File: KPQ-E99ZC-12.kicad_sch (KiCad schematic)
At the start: 23 parts, among them J1 USB, J2 Chassis, J3 SWD, J4 Edge Connector, J5 Alternate Connector, SW1 BOOT, U1 USBLC6-2SC6, U2 XC6206P332MR-G, U3 STM32C071KBT6

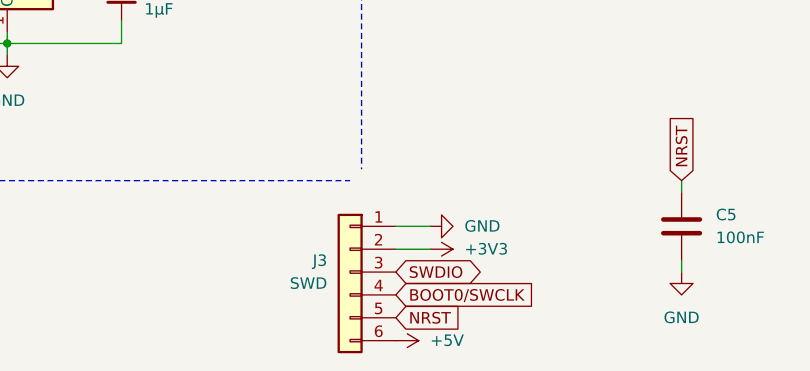
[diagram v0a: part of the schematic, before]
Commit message: Remove +5V from J3
This can be accessed via J1, and would avoid +5V being input from both J1 and J3 at the same time.
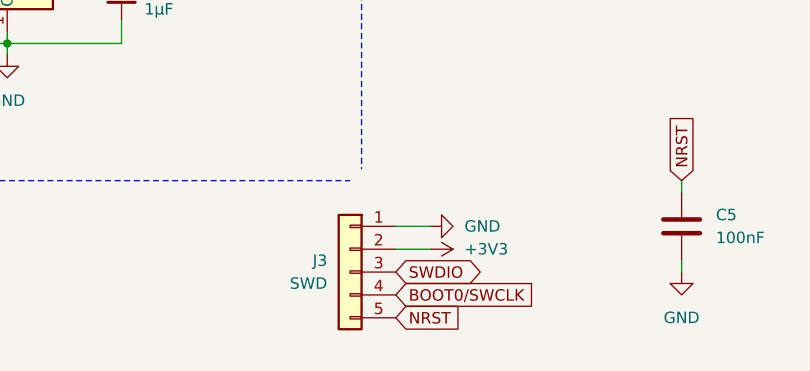
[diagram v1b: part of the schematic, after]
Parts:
- J3: footprint Connector_PinHeader_2.54mm:PinHeader_1x06_P2.54mm_Vertical -> Connector_PinHeader_2.54mm:PinHeader_1x05_P2.54mm_Vertical; symbol Connector_Generic:Conn_01x06 -> Connector_Generic:Conn_01x05; P6 +5V -> (none)
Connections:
- net +5V: no longer J3.6 (Pin_6)
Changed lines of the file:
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@@
-	)
-	(symbol
-		(lib_id "power:+5V")
-		(at 83.82 193.04 270)
-		(unit 1)
-		(exclude_from_sim no)
-		(in_bom yes)
-		(on_board yes)
-		(dnp no)
-		(fields_autoplaced yes)
-		(property "Reference" "#PWR032"
-			(at 80.01 193.04 0)
-			(effects
-				(font
-					(size 1.27 1.27)
-				)
-				(hide yes)
-			)
-		)
-		(property "Value" "+5V"
-			(at 87.63 193.04 90)
-			(effects
-				(font
-					(size 1.27 1.27)
-				)
-				(justify left)
-			)
-		)
-		(property "Footprint" ""
-			(at 83.82 193.04 0)
-			(effects
-				(font
-					(size 1.27 1.27)
-				)
-				(hide yes)
-			)
-		)
-		(property "Datasheet" ""
-			(at 83.82 193.04 0)
-			(effects
-				(font
-					(size 1.27 1.27)
-				)
-				(hide yes)
-			)
-		)
-		(property "Description" "Power symbol creates a global label with name \"+5V\""
-			(at 83.82 193.04 0)
-			(effects
-				(font
-					(size 1.27 1.27)
-				)
-				(hide yes)
-			)
-		)
-		(pin "1"
-		)
-		(instances
-			(project "KPQ-E99ZC-12"
-				(path "/2ca696f5-3b9d-4437-b6f7-98ba53a6592e"
-					(reference "#PWR032")
-					(unit 1)
-				)
-			)
-		)
 	)
 	(symbol
@@
 	)
 	(symbol
-		(lib_id "Connector_Generic:Conn_01x06")
+		(lib_id "Connector_Generic:Conn_01x05")
 		(at 78.74 185.42 0)
 		(mirror y)
@@
 			)
 		)
-		(property "Footprint" "Connector_PinHeader_2.54mm:PinHeader_1x06_P2.54mm_Vertical"
+		(property "Footprint" "Connector_PinHeader_2.54mm:PinHeader_1x05_P2.54mm_Vertical"
 			(at 78.74 185.42 0)
 			(effects
@@
 			)
 		)
-		(property "Description" "Generic connector, single row, 01x06, script generated (kicad-library-utils/schlib/autogen/connector/)"
+		(property "Description" "Generic connector, single row, 01x05, script generated (kicad-library-utils/schlib/autogen/connector/)"
 			(at 78.74 185.42 0)
 			(effects
@@
 			)
 		)
-		(property "P6" "+5V"
-			(at 78.74 185.42 0)
-			(effects
-				(font
-					(size 1.27 1.27)
-				)
-				(hide yes)
-			)
-		)
 		(pin "1"
 		)
@@
 		(pin "5"
 		)
-		(pin "6"
-		)
-		(instances
+		(instances

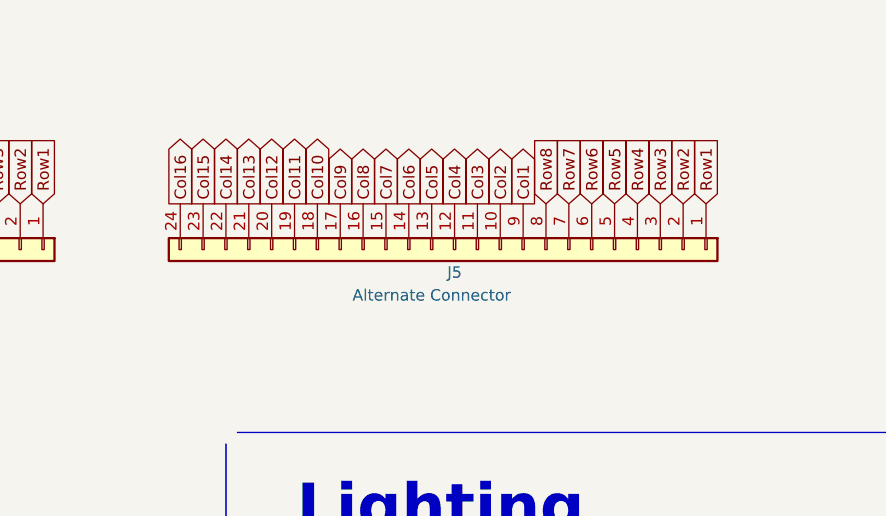
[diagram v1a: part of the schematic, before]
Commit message: Mark alternate connector as Do Not Populate
This is mainly so that it can be filtered out of the 3D view!
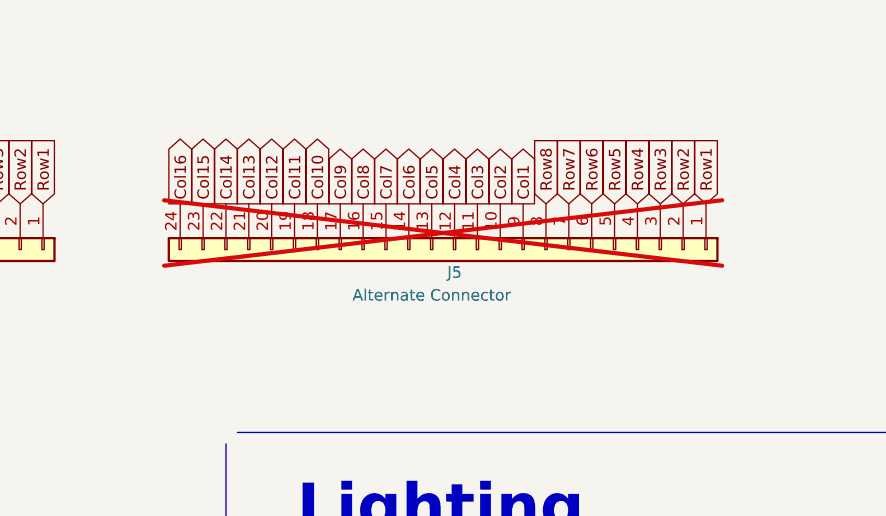
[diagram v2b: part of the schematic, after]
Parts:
- J5: now not fitted
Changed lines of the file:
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@@
 		(in_bom yes)
 		(on_board yes)
-		(dnp no)
+		(dnp yes)
 		(property "Reference" "J5"
 			(at 251.46 36.83 90)

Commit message: Add pin labelling to alternate connection
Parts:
- J3: footprint Connector_PinHeader_2.54mm:PinHeader_1x05_P2.54mm_Vertical -> Project_Library:PinHeader_1x05_P2.54mm_Vertical
- J5: footprint Connector_PinHeader_2.54mm:PinHeader_1x24_P2.54mm_Vertical -> Project_Library:PinHeader_1x24_P2.54mm_Vertical; P1 (none) -> A15; P10 (none) -> A0; P11 (none) -> A1; P12 (none) -> A2; P13 (none) -> A3; P14 (none) -> A4; P15 (none) -> A5; P16 (none) -> A6; P17 (none) -> A7; P18 (none) -> B0; P19 (none) -> B1; P2 (none) -> B3; P20 (none) -> B2; P21 (none) -> A8; P22 (none) -> A9; P23 (none) -> C6; P24 (none) -> A10; P3 (none) -> B4; P4 (none) -> B5; P5 (none) -> B6; P6 (none) -> B7; P7 (none) -> B8; P8 (none) -> C14; P9 (none) -> C15
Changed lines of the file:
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@@
 			)
 		)
-		(property "Footprint" "Connector_PinHeader_2.54mm:PinHeader_1x24_P2.54mm_Vertical"
+		(property "Footprint" "Project_Library:PinHeader_1x24_P2.54mm_Vertical"
 			(at 251.46 34.29 0)
 			(effects
@@
 		(property "Description" "Generic connector, single row, 01x24, script generated (kicad-library-utils/schlib/autogen/connector/)"
 			(at 251.46 34.29 0)
+			(effects
+				(font
+					(size 1.27 1.27)
+				)
+				(hide yes)
+			)
+		)
+		(property "P1" "A15"
+			(at 251.46 34.29 90)
+			(effects
+				(font
+					(size 1.27 1.27)
+				)
+				(hide yes)
+			)
+		)
+		(property "P2" "B3"
+			(at 251.46 34.29 90)
+			(effects
+				(font
+					(size 1.27 1.27)
+				)
+				(hide yes)
+			)
+		)
+		(property "P3" "B4"
+			(at 251.46 34.29 90)
+			(effects
+				(font
+					(size 1.27 1.27)
+				)
+				(hide yes)
+			)
+		)
+		(property "P4" "B5"
+			(at 251.46 34.29 90)
+			(effects
+				(font
+					(size 1.27 1.27)
+				)
+				(hide yes)
+			)
+		)
+		(property "P5" "B6"
+			(at 251.46 34.29 90)
+			(effects
+				(font
+					(size 1.27 1.27)
+				)
+				(hide yes)
+			)
+		)
+		(property "P6" "B7"
+			(at 251.46 34.29 90)
+			(effects
+				(font
+					(size 1.27 1.27)
+				)
+				(hide yes)
+			)
+		)
+		(property "P7" "B8"
+			(at 251.46 34.29 90)
+			(effects
+				(font
+					(size 1.27 1.27)
+				)
+				(hide yes)
+			)
+		)
+		(property "P8" "C14"
+			(at 251.46 34.29 90)
+			(effects
+				(font
+					(size 1.27 1.27)
+				)
+				(hide yes)
+			)
+		)
+		(property "P9" "C15"
+			(at 251.46 34.29 90)
+			(effects
+				(font
+					(size 1.27 1.27)
+				)
+				(hide yes)
+			)
+		)
+		(property "P10" "A0"
+			(at 251.46 34.29 90)
+			(effects
+				(font
+					(size 1.27 1.27)
+				)
+				(hide yes)
+			)
+		)
+		(property "P11" "A1"
+			(at 251.46 34.29 90)
+			(effects
+				(font
+					(size 1.27 1.27)
+				)
+				(hide yes)
+			)
+		)
+		(property "P12" "A2"
+			(at 251.46 34.29 90)
+			(effects
+				(font
+					(size 1.27 1.27)
+				)
+				(hide yes)
+			)
+		)
+		(property "P13" "A3"
+			(at 251.46 34.29 90)
+			(effects
+				(font
+					(size 1.27 1.27)
+				)
+				(hide yes)
+			)
+		)
+		(property "P14" "A4"
+			(at 251.46 34.29 90)
+			(effects
+				(font
+					(size 1.27 1.27)
+				)
+				(hide yes)
+			)
+		)
+		(property "P15" "A5"
+			(at 251.46 34.29 90)
+			(effects
+				(font
+					(size 1.27 1.27)
+				)
+				(hide yes)
+			)
+		)
+		(property "P16" "A6"
+			(at 251.46 34.29 90)
+			(effects
+				(font
+					(size 1.27 1.27)
+				)
+				(hide yes)
+			)
+		)
+		(property "P17" "A7"
+			(at 251.46 34.29 90)
+			(effects
+				(font
+					(size 1.27 1.27)
+				)
+				(hide yes)
+			)
+		)
+		(property "P18" "B0"
+			(at 251.46 34.29 90)
+			(effects
+				(font
+					(size 1.27 1.27)
+				)
+				(hide yes)
+			)
+		)
+		(property "P19" "B1"
+			(at 251.46 34.29 90)
+			(effects
+				(font
+					(size 1.27 1.27)
+				)
+				(hide yes)
+			)
+		)
+		(property "P20" "B2"
+			(at 251.46 34.29 90)
+			(effects
+				(font
+					(size 1.27 1.27)
+				)
+				(hide yes)
+			)
+		)
+		(property "P21" "A8"
+			(at 251.46 34.29 90)
+			(effects
+				(font
+					(size 1.27 1.27)
+				)
+				(hide yes)
+			)
+		)
+		(property "P22" "A9"
+			(at 251.46 34.29 90)
+			(effects
+				(font
+					(size 1.27 1.27)
+				)
+				(hide yes)
+			)
+		)
+		(property "P23" "C6"
+			(at 251.46 34.29 90)
+			(effects
+				(font
+					(size 1.27 1.27)
+				)
+				(hide yes)
+			)
+		)
+		(property "P24" "A10"
+			(at 251.46 34.29 90)
 			(effects
 				(font
@@
 			)
 		)
-		(property "Footprint" "Connector_PinHeader_2.54mm:PinHeader_1x05_P2.54mm_Vertical"
+		(property "Footprint" "Project_Library:PinHeader_1x05_P2.54mm_Vertical"
 			(at 78.74 185.42 0)
 			(effects

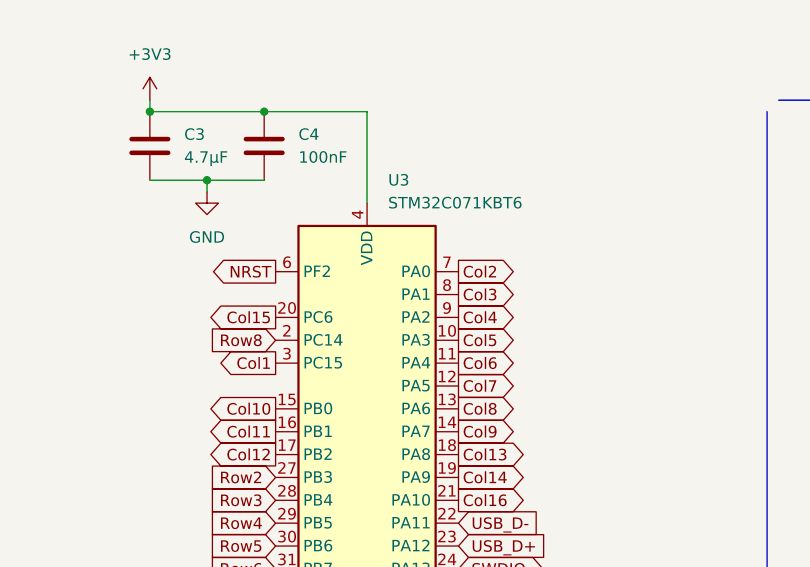
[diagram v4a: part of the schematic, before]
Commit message: Support STM32G0B1KBT6 in addition to STM32C071KBT6
The pin-out is the same, but the G0B1 datasheet says that pin PC13, PC14 and PC15 should not be used as outputs. The schematic is therefore updated to move Row 8 away from PC14. This requires a little rerouting, but nothing tricky.
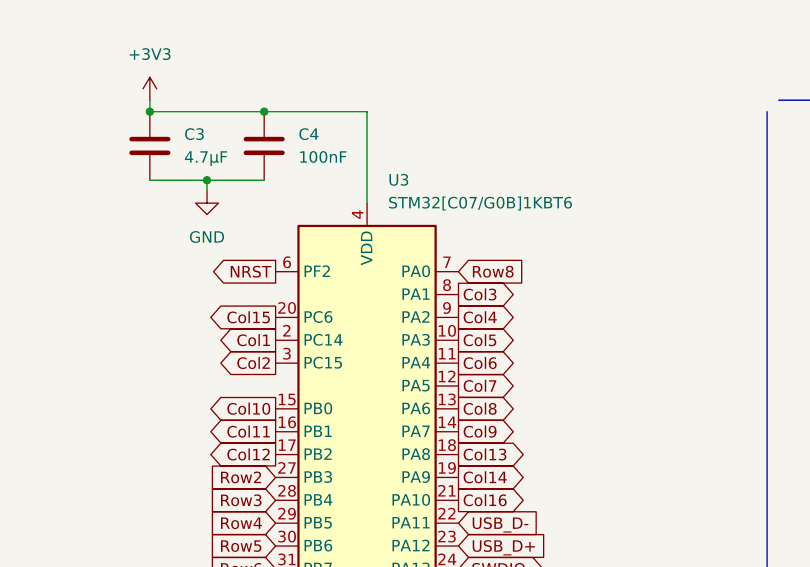
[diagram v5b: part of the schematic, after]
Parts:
- J5: P10 A0 -> C15; P8 C14 -> A0; P9 C15 -> C14
- U3: value STM32C071KBT6 -> STM32[C07/G0B]1KBT6
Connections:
- net Col1: now also U3.2 (PC14); no longer U3.3 (PC15)
- net Col2: now also U3.3 (PC15); no longer U3.7 (PA0)
- net Row8: now also U3.7 (PA0); no longer U3.2 (PC14)
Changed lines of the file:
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@@
 	(global_label "Col2"
 		(shape output)
-		(at 191.77 73.66 0)
+		(at 171.45 83.82 180)
 		(fields_autoplaced yes)
 		(effects
@@
 				(size 1.27 1.27)
 			)
-			(justify left)
+			(justify right)
 		)
 		(property "Intersheetrefs" "${INTERSHEET_REFS}"
-			(at 197.9858 73.66 0)
+			(at 165.2342 83.82 0)
 			(effects
 				(font
 					(size 1.27 1.27)
 				)
-				(justify left)
+				(justify right)
 				(hide yes)
 			)
@@
 	(global_label "Row8"
 		(shape input)
-		(at 171.45 81.28 180)
+		(at 191.77 73.66 0)
 		(fields_autoplaced yes)
 		(effects
@@
 				(size 1.27 1.27)
 			)
-			(justify right)
+			(justify left)
 		)
 		(property "Intersheetrefs" "${INTERSHEET_REFS}"
-			(at 164.2875 81.28 0)
+			(at 198.9325 73.66 0)
 			(effects
 				(font
 					(size 1.27 1.27)
 				)
-				(justify right)
+				(justify left)
 				(hide yes)
 			)
@@
 	(global_label "Col1"
 		(shape output)
-		(at 171.45 83.82 180)
+		(at 171.45 81.28 180)
 		(fields_autoplaced yes)
 		(effects
@@
 		)
 		(property "Intersheetrefs" "${INTERSHEET_REFS}"
-			(at 165.336 83.82 0)
+			(at 165.336 81.28 0)
 			(effects
 				(font
@@
 			)
 		)
-		(property "Value" "STM32C071KBT6"
+		(property "Value" "STM32[C07/G0B]1KBT6"
 			(at 183.9471 66.04 0)
 			(effects
@@
 			)
 		)
-		(property "P8" "C14"
+		(property "P8" "A0"
 			(at 251.46 34.29 90)
 			(effects
@@
 			)
 		)
-		(property "P9" "C15"
+		(property "P9" "C14"
 			(at 251.46 34.29 90)
 			(effects
@@
 			)
 		)
-		(property "P10" "A0"
+		(property "P10" "C15"
 			(at 251.46 34.29 90)
 			(effects
